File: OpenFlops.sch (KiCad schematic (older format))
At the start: 61 parts, among them J7 DISPLAY_PORT, P1 FLOPPY_CONN, P2 POWER_INPUT, P3 USB_A_FEMALE, P4 PROG_PORT, P5 JUMPERS, Q1 MOS_N_GSD, Q2 MOS_N_GSD, Q3 MOS_N_GSD, Q4 MOS_N_GSD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

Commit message: And we're done! This is a first rev of the PCB, done "by eye" as similarly as possible as one of my boards. There are quite a few improvements that we can make...
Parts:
- P3: footprint Connector_USB:USB_A_Molex_105057_Vertical -> OpenFlops:USB_A_FEMALE
- S3, S4: footprint (none) -> OpenFlops:PUSH_BUTTON_RIGHT_ANGLE
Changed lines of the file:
@@
 EESchema Schematic File Version 4
+LIBS:OpenFlops-cache
 EELAYER 29 0
 EELAYER END
@@
 F 0 "S3" H 1125 3885 50  0000 C CNN
 F 1 "BT_RIGHT" H 1125 3794 50  0000 C CNN
-F 2 "" H 1125 3800 50  0001 C CNN
+F 2 "OpenFlops:PUSH_BUTTON_RIGHT_ANGLE" H 1125 3800 50  0001 C CNN
 F 3 "~" H 1125 3800 50  0001 C CNN
 	1    1125 3600
@@
 F 0 "S4" H 1125 3707 50  0000 C CNN
 F 1 "BT_LEFT" H 1125 3616 50  0000 C CNN
-F 2 "" H 1125 4000 50  0001 C CNN
+F 2 "OpenFlops:PUSH_BUTTON_RIGHT_ANGLE" H 1125 4000 50  0001 C CNN
 F 3 "~" H 1125 4000 50  0001 C CNN
 	1    1125 3800
@@
 F 0 "P3" H 7835 1039 50  0000 R CNN
 F 1 "USB_A_FEMALE" H 7835 948 50  0000 R CNN
-F 2 "Connector_USB:USB_A_Molex_105057_Vertical" H 8215 1000 50  0001 C CNN
+F 2 "OpenFlops:USB_A_FEMALE" H 8215 1000 50  0001 C CNN
 F 3 " ~" H 8215 1000 50  0001 C CNN
 	1    8065 1050

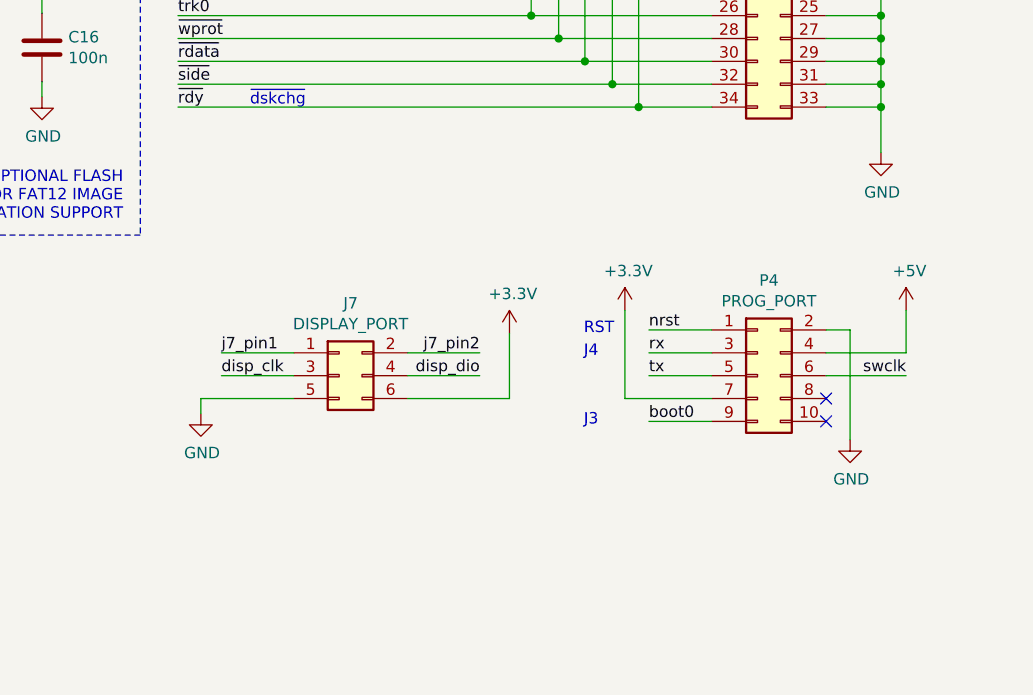
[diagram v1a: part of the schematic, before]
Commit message: Add mounting holes and several refinements
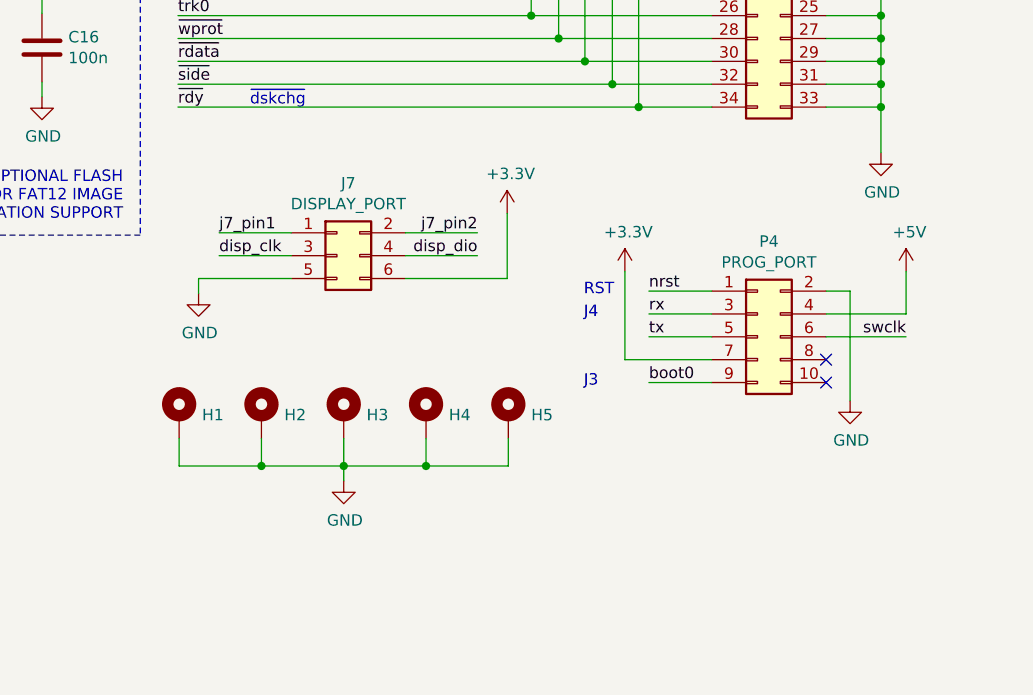
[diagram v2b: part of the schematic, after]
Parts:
- added H1, H2, H3, H4, H5: MountingHole_Pad, OpenFlops:MountingHole_M3_Pad, symbol Mechanical:MountingHole_Pad
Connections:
- net GND: now also H1.1, H2.1, H3.1, H4.1, H5.1
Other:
- moved on the sheet: J7, P4

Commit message: Put power connectors on spare P4 pins
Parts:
- J7: footprint Connector_PinHeader_2.54mm:PinHeader_2x03_P2.54mm_Horizontal -> Connector_PinHeader_2.54mm:PinHeader_2x03_P2.54mm_Vertical
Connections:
- net +3V3: now also P4.10 (Pin_10)
- net GND: now also P4.6 (Pin_6), P4.8 (Pin_8)
- net swclk: no longer P4.6 (Pin_6)
- no-connect marks 24 -> 22
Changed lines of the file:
@@
 Text Notes 9280 5435 0    50   ~ 0
 RST
-Wire Wire Line
-	10690 5610 10340 5610
-Text Label 10690 5610 2    50   ~ 0
-swclk
 Text Label 8815 5255 2    50   ~ 0
 disp_dio
@@
 F 0 "J7" H 8250 5572 50  0000 C CNN
 F 1 "DISPLAY_PORT" H 8250 5481 50  0000 C CNN
-F 2 "Connector_PinHeader_2.54mm:PinHeader_2x03_P2.54mm_Horizontal" H 8200 5255 50  0001 C CNN
+F 2 "Connector_PinHeader_2.54mm:PinHeader_2x03_P2.54mm_Vertical" H 8200 5255 50  0001 C CNN
 F 3 "~" H 8200 5255 50  0001 C CNN
 	1    8200 5255
@@
 $EndComp
 Wire Wire Line
-	10445 5410 10445 5890
+	10445 5410 10445 5610
 Wire Wire Line
 	10340 5410 10445 5410
-NoConn ~ 10340 5810
-NoConn ~ 10340 5710
 $Comp
 L Connector_Generic:Conn_02x05_Odd_Even P4
@@
 Wire Wire Line
 	8230 6175 8590 6175
+Wire Wire Line
+	10340 5610 10445 5610
+Connection ~ 10445 5610
+Wire Wire Line
+	10445 5610 10445 5710
+Wire Wire Line
+	10340 5710 10445 5710
+Connection ~ 10445 5710
+Wire Wire Line
+	10445 5710 10445 5890
+$Comp
+L power:+3.3V #PWR0143
+U 1 1 5D5DDDC2
+P 10875 5325
+F 0 "#PWR0143" H 10875 5175 50  0001 C CNN
+F 1 "+3.3V" H 10890 5498 50  0000 C CNN
+F 2 "" H 10875 5325 50  0001 C CNN
+F 3 "" H 10875 5325 50  0001 C CNN
+	1    10875 5325
+	1    0    0    -1
+$EndComp
+Wire Wire Line
+	10875 5325 10875 5810
+Wire Wire Line
+	10875 5810 10340 5810
 $EndSCHEMATC

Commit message: Make this an enhanced drive for FlashFloppy
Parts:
- removed C16: 100n, Capacitor_SMD:C_0805_2012Metric_Pad1.15x1.40mm_HandSolder, symbol Device:C
- removed J7: DISPLAY_PORT, Connector_PinHeader_2.54mm:PinHeader_2x03_P2.54mm_Vertical, symbol Connector_Generic:Conn_02x03_Odd_Even
- removed L35: LED_RED, LED_THT:LED_D3.0mm-3, symbol Device:LED_Dual_CAC
- removed U8: W25Q32JVSS (?), Package_SO:SOIC-8_5.23x5.23mm_P1.27mm, symbol Memory_Flash:W25Q32JVSS
- added LD2: LED_RED, LED_THT:LED_D3.0mm, symbol Device:LED
- added P6: ENCODER_PORT, symbol Connector_Generic:Conn_01x05
- added P7: DISPLAY_PORT, symbol Connector_Generic:Conn_01x04
- added PU14, PU15: 1k, Resistor_SMD:R_0805_2012Metric_Pad1.15x1.40mm_HandSolder, symbol Device:R
- added Q7: 2N3904, Package_TO_SOT_THT:TO-92_Inline, symbol Transistor_BJT:2N3904
- added R3, R4: 3.3K, Resistor_SMD:R_0805_2012Metric_Pad1.15x1.40mm_HandSolder, symbol Device:R
- added R5: 1K, Resistor_SMD:R_0805_2012Metric_Pad1.15x1.40mm_HandSolder, symbol Device:R
- added SPK1: Speaker, symbol Device:Speaker
- renumbered L4 to LD1
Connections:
- net labels added: enc_clk, enc_dt, ~sely
- net labels removed: j7_pin1, j7_pin2
- wire segments 376 -> 399
- no-connect marks 22 -> 21
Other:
- note added: "DRV1 - S0"
- note added: "DRV1 - S1"
- note added: "DRV2 - S0"
- note added: "DRV2 - S1"
- note added: "ENHANCED\nGOTEK,\nNO SD\nSUPPORT"
- note added: "OPTIONAL I2C\nBUS PULL-UPS"
- note removed: "JA"
- note removed: "JB"
- note removed: "OPTIONAL FLASH\nFOR FAT12 IMAGE\nCREATION SUPPORT"
- note removed: "S0"
- note removed: "S1"
- moved on the sheet: C6, C7, C8, C9, P5, PU4, R20

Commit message: Add current-limiting resistor on speaker
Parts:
- added R6: 100, Resistor_SMD:R_0805_2012Metric_Pad1.15x1.40mm_HandSolder, symbol Device:R
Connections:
- wire segments 399 -> 400
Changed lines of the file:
@@
 	4995 4100 4915 4100
 Wire Wire Line
-	4915 4100 4915 4020
+	4915 3685 4915 3635
 $Comp
 L power:+5V #PWR0137
 U 1 1 5D4C0625
-P 4915 4020
-F 0 "#PWR0137" H 4915 3870 50  0001 C CNN
-F 1 "+5V" H 4930 4193 50  0000 C CNN
-F 2 "" H 4915 4020 50  0001 C CNN
-F 3 "" H 4915 4020 50  0001 C CNN
-	1    4915 4020
+P 4915 3635
+F 0 "#PWR0137" H 4915 3485 50  0001 C CNN
+F 1 "+5V" H 4930 3808 50  0000 C CNN
+F 2 "" H 4915 3635 50  0001 C CNN
+F 3 "" H 4915 3635 50  0001 C CNN
+	1    4915 3635
 	1    0    0    -1
 $EndComp
@@
 Wire Wire Line
 	4465 785  4550 785
+$Comp
+L Device:R R6
+U 1 1 5E2368C4
+P 4915 3835
+F 0 "R6" H 4905 3690 50  0000 R CNN
+F 1 "100" V 4910 3910 50  0000 R CNN
+F 2 "Resistor_SMD:R_0805_2012Metric_Pad1.15x1.40mm_HandSolder" V 4845 3835 50  0001 C CNN
+F 3 "~" H 4915 3835 50  0001 C CNN
+	1    4915 3835
+	-1   0    0    1
+$EndComp
+Wire Wire Line
+	4915 3985 4915 4100
 $EndSCHEMATC

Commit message: Add protection diode on speaker. Thanks Brian Allan
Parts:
- added D2: 1N5819 (?), Diode_SMD:D_SOD-123, symbol Device:D
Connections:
- wire segments 400 -> 406
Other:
- moved on the sheet: R6, SPK1
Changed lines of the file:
@@
 L Device:Speaker SPK1
 U 1 1 5D494B63
-P 5195 4100
-F 0 "SPK1" H 5365 4096 50  0000 L CNN
-F 1 "Speaker" H 5365 4005 50  0000 L CNN
-F 2 "" H 5195 3900 50  0001 C CNN
-F 3 "~" H 5185 4050 50  0001 C CNN
-	1    5195 4100
-	1    0    0    -1
-$EndComp
-Wire Wire Line
-	4995 4100 4915 4100
-Wire Wire Line
-	4915 3685 4915 3635
+P 5190 4015
+F 0 "SPK1" H 5360 4011 50  0000 L CNN
+F 1 "Speaker" H 5360 3920 50  0000 L CNN
+F 2 "" H 5190 3815 50  0001 C CNN
+F 3 "~" H 5180 3965 50  0001 C CNN
+	1    5190 4015
+	1    0    0    -1
+$EndComp
+Wire Wire Line
+	4990 4015 4915 4015
+Wire Wire Line
+	4915 3550 4915 3500
 $Comp
 L power:+5V #PWR0137
 U 1 1 5D4C0625
-P 4915 3635
-F 0 "#PWR0137" H 4915 3485 50  0001 C CNN
-F 1 "+5V" H 4930 3808 50  0000 C CNN
-F 2 "" H 4915 3635 50  0001 C CNN
-F 3 "" H 4915 3635 50  0001 C CNN
-	1    4915 3635
+P 4915 3500
+F 0 "#PWR0137" H 4915 3350 50  0001 C CNN
+F 1 "+5V" H 4930 3673 50  0000 C CNN
+F 2 "" H 4915 3500 50  0001 C CNN
+F 3 "" H 4915 3500 50  0001 C CNN
+	1    4915 3500
 	1    0    0    -1
 $EndComp
@@
 $EndComp
 Wire Wire Line
-	4995 4200 4915 4200
-Wire Wire Line
-	4915 4200 4915 4285
+	4990 4115 4915 4115
+Wire Wire Line
+	4915 4115 4915 4265
 $Comp
 L power:GND #PWR0138
@@
 L Device:R R6
 U 1 1 5E2368C4
-P 4915 3835
-F 0 "R6" H 4905 3690 50  0000 R CNN
-F 1 "100" V 4910 3910 50  0000 R CNN
-F 2 "Resistor_SMD:R_0805_2012Metric_Pad1.15x1.40mm_HandSolder" V 4845 3835 50  0001 C CNN
-F 3 "~" H 4915 3835 50  0001 C CNN
-	1    4915 3835
+P 4915 3700
+F 0 "R6" H 4905 3555 50  0000 R CNN
+F 1 "100" V 4910 3775 50  0000 R CNN
+F 2 "Resistor_SMD:R_0805_2012Metric_Pad1.15x1.40mm_HandSolder" V 4845 3700 50  0001 C CNN
+F 3 "~" H 4915 3700 50  0001 C CNN
+	1    4915 3700
 	-1   0    0    1
 $EndComp
 Wire Wire Line
-	4915 3985 4915 4100
+	4915 3850 4915 3890
+Wire Wire Line
+	4730 3925 4730 3890
+Wire Wire Line
+	4730 3890 4915 3890
+Connection ~ 4915 3890
+Wire Wire Line
+	4915 3890 4915 4015
+Wire Wire Line
+	4730 4225 4730 4265
+Wire Wire Line
+	4730 4265 4915 4265
+Connection ~ 4915 4265
+Wire Wire Line
+	4915 4265 4915 4285
+$Comp
+L Device:D D2
+U 1 1 5E2F4A52
+P 4730 4075
+F 0 "D2" V 4684 4154 50  0000 L CNN
+F 1 "1N5819 (?)" V 4775 4154 50  0000 L CNN
+F 2 "Diode_SMD:D_SOD-123" H 4730 4075 50  0001 C CNN
+F 3 "~" H 4730 4075 50  0001 C CNN
+	1    4730 4075
+	0    -1   1    0
+$EndComp
 $EndSCHEMATC

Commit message: Update PCB
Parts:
- removed Q7: 2N3904, Package_TO_SOT_THT:TO-92_Inline, symbol Transistor_BJT:2N3904
- added Q7: MMBT3904, Package_TO_SOT_SMD:SOT-23_Handsoldering, symbol Transistor_BJT:MMBT3904
- P6: footprint (none) -> Connector_PinHeader_2.54mm:PinHeader_1x05_P2.54mm_Vertical
- P7: footprint (none) -> Connector_PinHeader_2.54mm:PinHeader_1x04_P2.54mm_Vertical
- SPK1: footprint (none) -> OpenFlops:Buzzer
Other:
- moved on the sheet: D2, R5, R6, SPK1
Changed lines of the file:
@@
 L Device:Speaker SPK1
 U 1 1 5D494B63
-P 5190 4015
-F 0 "SPK1" H 5360 4011 50  0000 L CNN
-F 1 "Speaker" H 5360 3920 50  0000 L CNN
-F 2 "" H 5190 3815 50  0001 C CNN
-F 3 "~" H 5180 3965 50  0001 C CNN
-	1    5190 4015
-	1    0    0    -1
-$EndComp
-Wire Wire Line
-	4990 4015 4915 4015
-Wire Wire Line
-	4915 3550 4915 3500
+P 5180 4185
+F 0 "SPK1" H 5350 4181 50  0000 L CNN
+F 1 "Speaker" H 5350 4090 50  0000 L CNN
+F 2 "OpenFlops:Buzzer" H 5180 3985 50  0001 C CNN
+F 3 "~" H 5170 4135 50  0001 C CNN
+	1    5180 4185
+	1    0    0    -1
+$EndComp
+Wire Wire Line
+	4980 4185 4905 4185
+Wire Wire Line
+	4905 3720 4905 3670
 $Comp
 L power:+5V #PWR0137
 U 1 1 5D4C0625
-P 4915 3500
-F 0 "#PWR0137" H 4915 3350 50  0001 C CNN
-F 1 "+5V" H 4930 3673 50  0000 C CNN
-F 2 "" H 4915 3500 50  0001 C CNN
-F 3 "" H 4915 3500 50  0001 C CNN
-	1    4915 3500
-	1    0    0    -1
-$EndComp
-$Comp
-L Transistor_BJT:2N3904 Q7
-U 1 1 5D4C20E2
-P 4815 4485
-F 0 "Q7" H 5005 4531 50  0000 L CNN
-F 1 "2N3904" H 5005 4440 50  0000 L CNN
-F 2 "Package_TO_SOT_THT:TO-92_Inline" H 5015 4410 50  0001 L CIN
-F 3 "https://www.fairchildsemi.com/datasheets/2N/2N3904.pdf" H 4815 4485 50  0001 L CNN
-	1    4815 4485
-	1    0    0    -1
-$EndComp
-Wire Wire Line
-	4990 4115 4915 4115
-Wire Wire Line
-	4915 4115 4915 4265
+P 4905 3670
+F 0 "#PWR0137" H 4905 3520 50  0001 C CNN
+F 1 "+5V" H 4920 3843 50  0000 C CNN
+F 2 "" H 4905 3670 50  0001 C CNN
+F 3 "" H 4905 3670 50  0001 C CNN
+	1    4905 3670
+	1    0    0    -1
+$EndComp
+Wire Wire Line
+	4980 4285 4905 4285
 $Comp
 L power:GND #PWR0138
 U 1 1 5D4EFD9D
-P 4915 4750
-F 0 "#PWR0138" H 4915 4500 50  0001 C CNN
-F 1 "GND" H 4920 4577 50  0000 C CNN
-F 2 "" H 4915 4750 50  0001 C CNN
-F 3 "" H 4915 4750 50  0001 C CNN
-	1    4915 4750
-	1    0    0    -1
-$EndComp
-Wire Wire Line
-	4915 4685 4915 4750
+P 4905 4920
+F 0 "#PWR0138" H 4905 4670 50  0001 C CNN
+F 1 "GND" H 4910 4747 50  0000 C CNN
+F 2 "" H 4905 4920 50  0001 C CNN
+F 3 "" H 4905 4920 50  0001 C CNN
+	1    4905 4920
+	1    0    0    -1
+$EndComp
+Wire Wire Line
+	4905 4855 4905 4920
 $Comp
 L Device:R R5
 U 1 1 5D51C5E8
-P 4385 4485
-F 0 "R5" V 4480 4485 50  0000 C CNN
-F 1 "1K" V 4385 4485 50  0000 C CNN
-F 2 "Resistor_SMD:R_0805_2012Metric_Pad1.15x1.40mm_HandSolder" V 4315 4485 50  0001 C CNN
-F 3 "~" H 4385 4485 50  0001 C CNN
-	1    4385 4485
+P 4375 4655
+F 0 "R5" V 4470 4655 50  0000 C CNN
+F 1 "1K" V 4375 4655 50  0000 C CNN
+F 2 "Resistor_SMD:R_0805_2012Metric_Pad1.15x1.40mm_HandSolder" V 4305 4655 50  0001 C CNN
+F 3 "~" H 4375 4655 50  0001 C CNN
+	1    4375 4655
 	0    1    1    0
 $EndComp
 Wire Wire Line
-	4535 4485 4615 4485
-Wire Wire Line
-	4235 4485 4065 4485
-Text Label 4065 4485 0    50   ~ 0
+	4525 4655 4605 4655
+Wire Wire Line
+	4225 4655 4055 4655
+Text Label 4055 4655 0    50   ~ 0
 jb
 $Comp
@@
 F 0 "P7" H 7553 4925 50  0000 C CNN
 F 1 "DISPLAY_PORT" H 7553 5016 50  0000 C CNN
-F 2 "" H 7635 5350 50  0001 C CNN
+F 2 "Connector_PinHeader_2.54mm:PinHeader_1x04_P2.54mm_Vertical" H 7635 5350 50  0001 C CNN
 F 3 "~" H 7635 5350 50  0001 C CNN
 	1    7635 5350
@@
 F 0 "P6" H 6018 4165 50  0000 C CNN
 F 1 "ENCODER_PORT" H 6018 4256 50  0000 C CNN
-F 2 "" H 6100 4590 50  0001 C CNN
+F 2 "Connector_PinHeader_2.54mm:PinHeader_1x05_P2.54mm_Vertical" H 6100 4590 50  0001 C CNN
 F 3 "~" H 6100 4590 50  0001 C CNN
 	1    6100 4590
@@
 L Device:R R6
 U 1 1 5E2368C4
-P 4915 3700
-F 0 "R6" H 4905 3555 50  0000 R CNN
-F 1 "100" V 4910 3775 50  0000 R CNN
-F 2 "Resistor_SMD:R_0805_2012Metric_Pad1.15x1.40mm_HandSolder" V 4845 3700 50  0001 C CNN
-F 3 "~" H 4915 3700 50  0001 C CNN
-	1    4915 3700
+P 4905 3870
+F 0 "R6" H 4895 3725 50  0000 R CNN
+F 1 "100" V 4900 3945 50  0000 R CNN
+F 2 "Resistor_SMD:R_0805_2012Metric_Pad1.15x1.40mm_HandSolder" V 4835 3870 50  0001 C CNN
+F 3 "~" H 4905 3870 50  0001 C CNN
+	1    4905 3870
 	-1   0    0    1
 $EndComp
 Wire Wire Line
-	4915 3850 4915 3890
-Wire Wire Line
-	4730 3925 4730 3890
-Wire Wire Line
-	4730 3890 4915 3890
-Connection ~ 4915 3890
-Wire Wire Line
-	4915 3890 4915 4015
-Wire Wire Line
-	4730 4225 4730 4265
-Wire Wire Line
-	4730 4265 4915 4265
-Connection ~ 4915 4265
-Wire Wire Line
-	4915 4265 4915 4285
+	4905 4020 4905 4060
+Wire Wire Line
+	4720 4095 4720 4060
+Wire Wire Line
+	4720 4060 4905 4060
+Connection ~ 4905 4060
+Wire Wire Line
+	4905 4060 4905 4185
+Wire Wire Line
+	4720 4395 4720 4435
 $Comp
 L Device:D D2
 U 1 1 5E2F4A52
-P 4730 4075
-F 0 "D2" V 4684 4154 50  0000 L CNN
-F 1 "1N5819 (?)" V 4775 4154 50  0000 L CNN
-F 2 "Diode_SMD:D_SOD-123" H 4730 4075 50  0001 C CNN
-F 3 "~" H 4730 4075 50  0001 C CNN
-	1    4730 4075
+P 4720 4245
+F 0 "D2" V 4674 4324 50  0000 L CNN
+F 1 "1N5819 (?)" V 4765 4324 50  0000 L CNN
+F 2 "Diode_SMD:D_SOD-123" H 4720 4245 50  0001 C CNN
+F 3 "~" H 4720 4245 50  0001 C CNN
+	1    4720 4245
 	0    -1   1    0
 $EndComp
+$Comp
+L Transistor_BJT:MMBT3904 Q7
+U 1 1 5E577975
+P 4805 4655
+F 0 "Q7" H 4996 4701 50  0000 L CNN
+F 1 "MMBT3904" H 4996 4610 50  0000 L CNN
+F 2 "Package_TO_SOT_SMD:SOT-23_Handsoldering" H 5005 4580 50  0001 L CIN
+F 3 "https://www.fairchildsemi.com/datasheets/2N/2N3904.pdf" H 4805 4655 50  0001 L CNN
+	1    4805 4655
+	1    0    0    -1
+$EndComp
+Wire Wire Line
+	4905 4285 4905 4435
+Wire Wire Line
+	4720 4435 4905 4435
+Connection ~ 4905 4435
+Wire Wire Line
+	4905 4435 4905 4455
 $EndSCHEMATC
